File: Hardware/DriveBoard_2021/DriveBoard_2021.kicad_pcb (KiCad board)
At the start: 2 copper layers, 124.5 x 101.6 mm, 91 parts, among them U1 LM2576S-3.3, U2 LM2576HVS-5, U3 TM4C129E_Launchpad, U4 MCP2551-I-SN

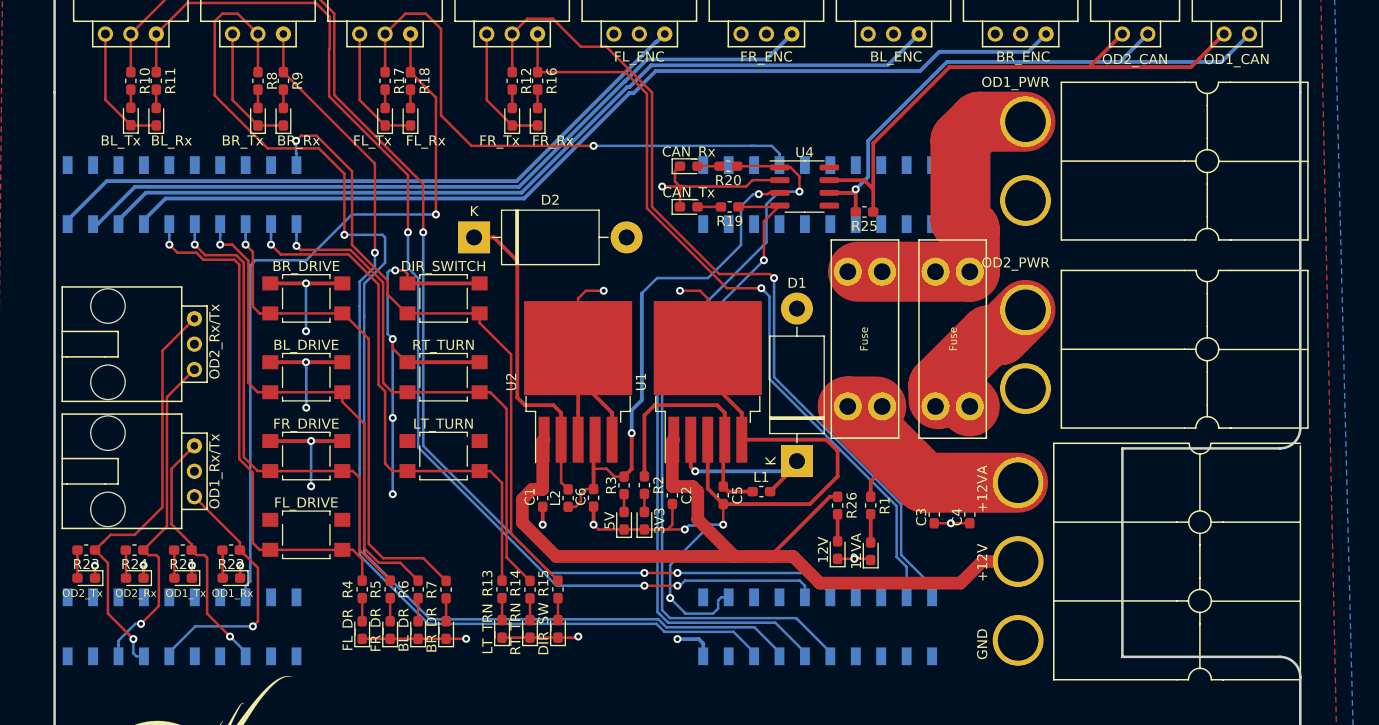
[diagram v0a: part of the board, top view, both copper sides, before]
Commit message: Switched TIVA SMD bottom to THT. Moved Odrive Andersons and re-traced pwr. Added names to LEDs.
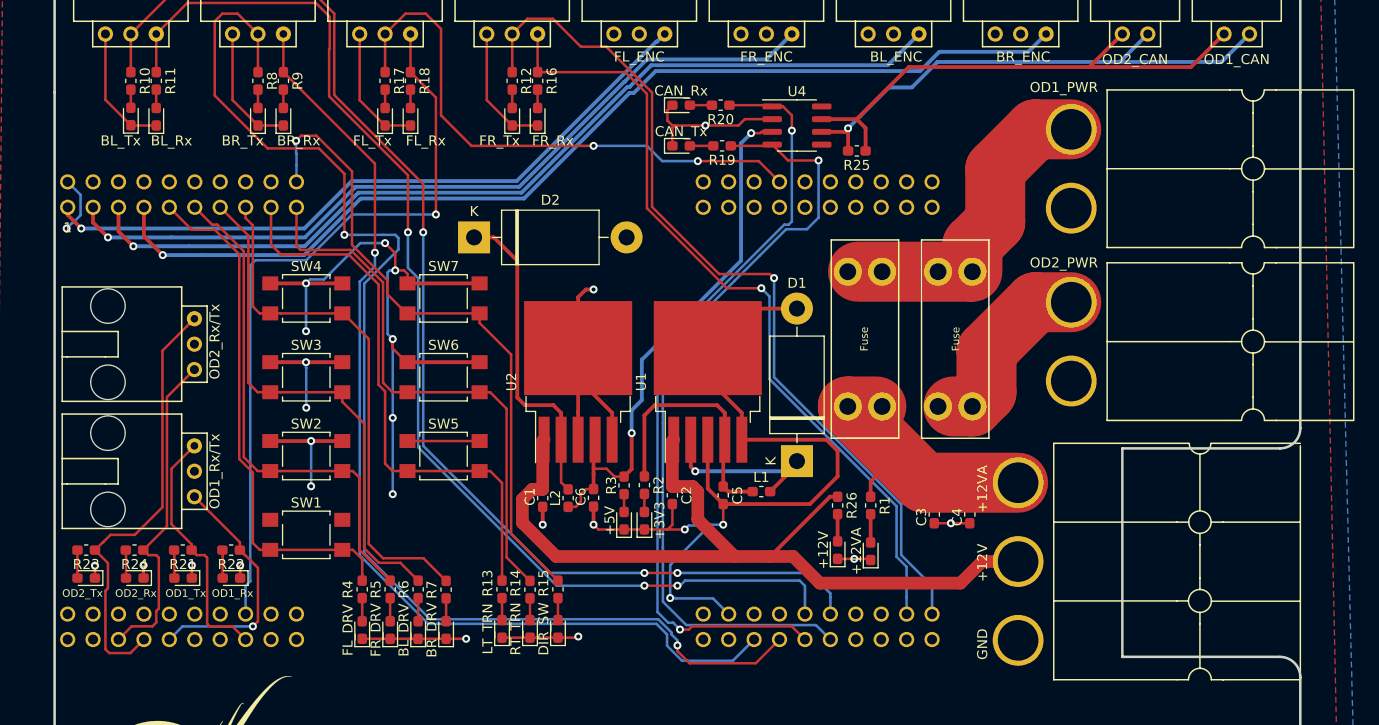
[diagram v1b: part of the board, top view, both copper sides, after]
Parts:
- U3: footprint MRDT_Shields:TM4C129E_Launchpad_FULL_SMD_BOTTOM -> MRDT_Shields:TM4C129E_Launchpad_FULL_THT_BOTTOM
- moved CAN_Tx 6.14 mm to (132.4, 76.7)
- moved R19 6.14 mm to (136.5, 76.7)
- moved R25 6.14 mm to (150.0, 77.2)
- moved U4 6.14 mm to (144.0, 74.7)
- moved CAN_Rx 6.14 mm to (132.4, 72.6)
- moved R20 6.14 mm to (136.4, 72.6)
- moved Conn2 4.64 mm to (175.0, 71.1)
- moved Conn3 4.64 mm to (175.0, 88.4)
- moved F2 0.25 mm to (156.5, 86.1)
- renumbered 12V to +12V, 12VA to +12VA, 3V3 to +3V3, 5V to +5V, BL_DR to BL_DRV, BR_DR to BR_DRV, FL_DR to FL_DRV, FR_DR to FR_DRV, FL_DRIVE to SW1, FR_DRIVE to SW2, BL_DRIVE to SW3, BR_DRIVE to SW4, LT_TURN to SW5, RT_TURN to SW6, DIR_SWITCH to SW7
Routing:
- net +3V3: track 107.8 -> 123.7 mm
- net CAN_Tx: track 68.4 -> 79.6 mm
- net BR_PWM: track 98.2 -> 103.0 mm, vias 0 -> 1
- net GND: track 214.6 -> 219.1 mm
- net CAN_Rx: track 74.0 -> 78.2 mm, vias 1 -> 2
- net CANH: track 55.9 -> 51.9 mm
- net CANL: track 56.9 -> 53.0 mm
- net BL_PWM: track 88.1 -> 91.8 mm, vias 0 -> 1
- net BR_Tx: track 121.6 -> 125.2 mm, vias 1 -> 2
- net FR_PWM: track 77.7 -> 80.4 mm, vias 0 -> 1
- net +5V: track 51.4 -> 53.8 mm
- net OD2_Tx: track 41.7 -> 43.8 mm, vias 1 -> 0
- net RT_TURN: track 54.0 -> 55.6 mm, vias 1 -> 0
- net LT_TURN: track 54.9 -> 56.5 mm, vias 1 -> 0
- net FR_Tx: track 86.5 -> 88.1 mm
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
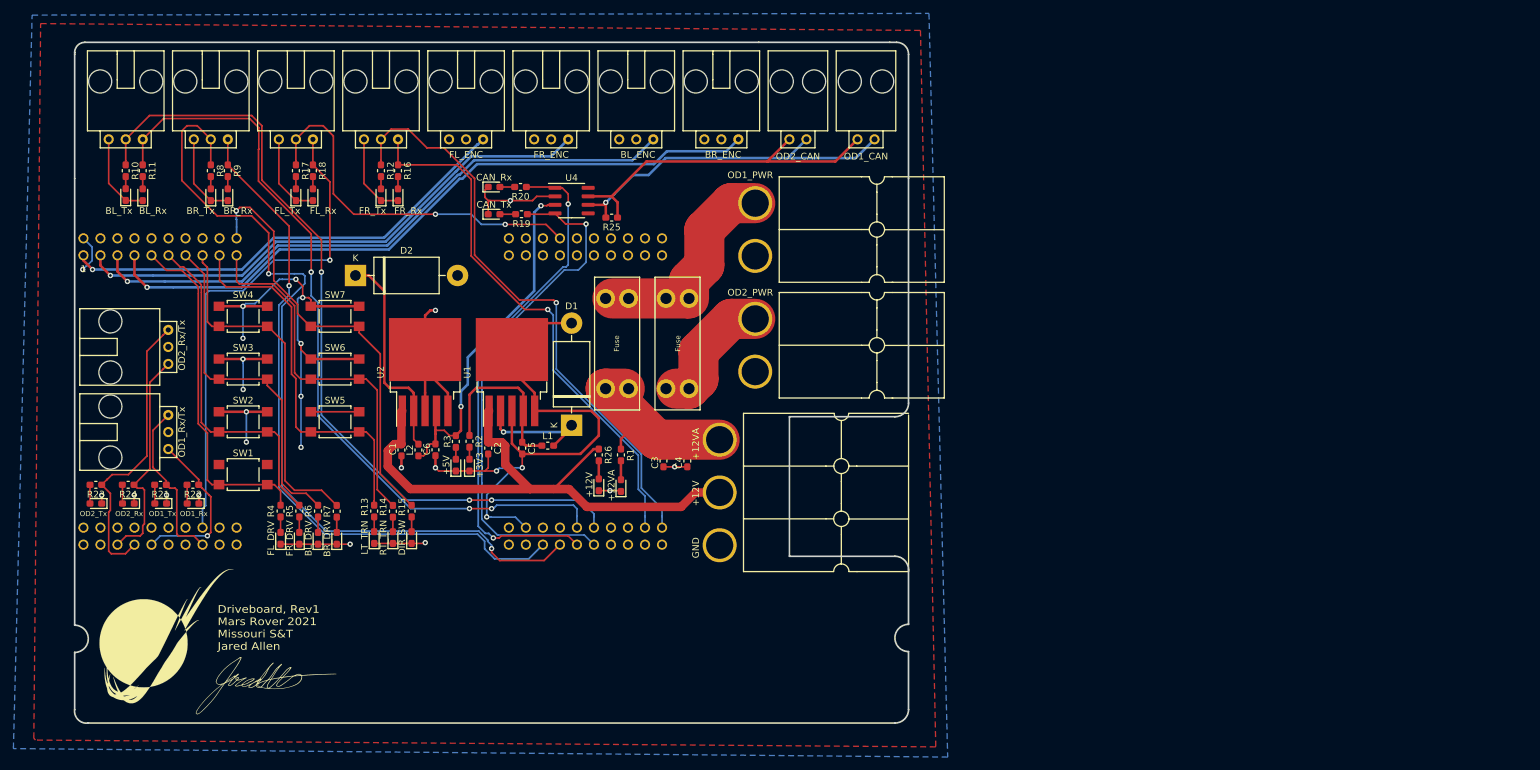
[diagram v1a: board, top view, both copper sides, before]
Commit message: Initial Board Overhaul. Power switched to Okis, re-routing of traces to easier paths. Additional changes.
LEDs given better groupings and silkscreen tags. Given new room with the switch to Okis for regualtors, traces were re-routed to ease the complexity of the board. Odrive trace size changed to 350mil to handle 30A actuation.
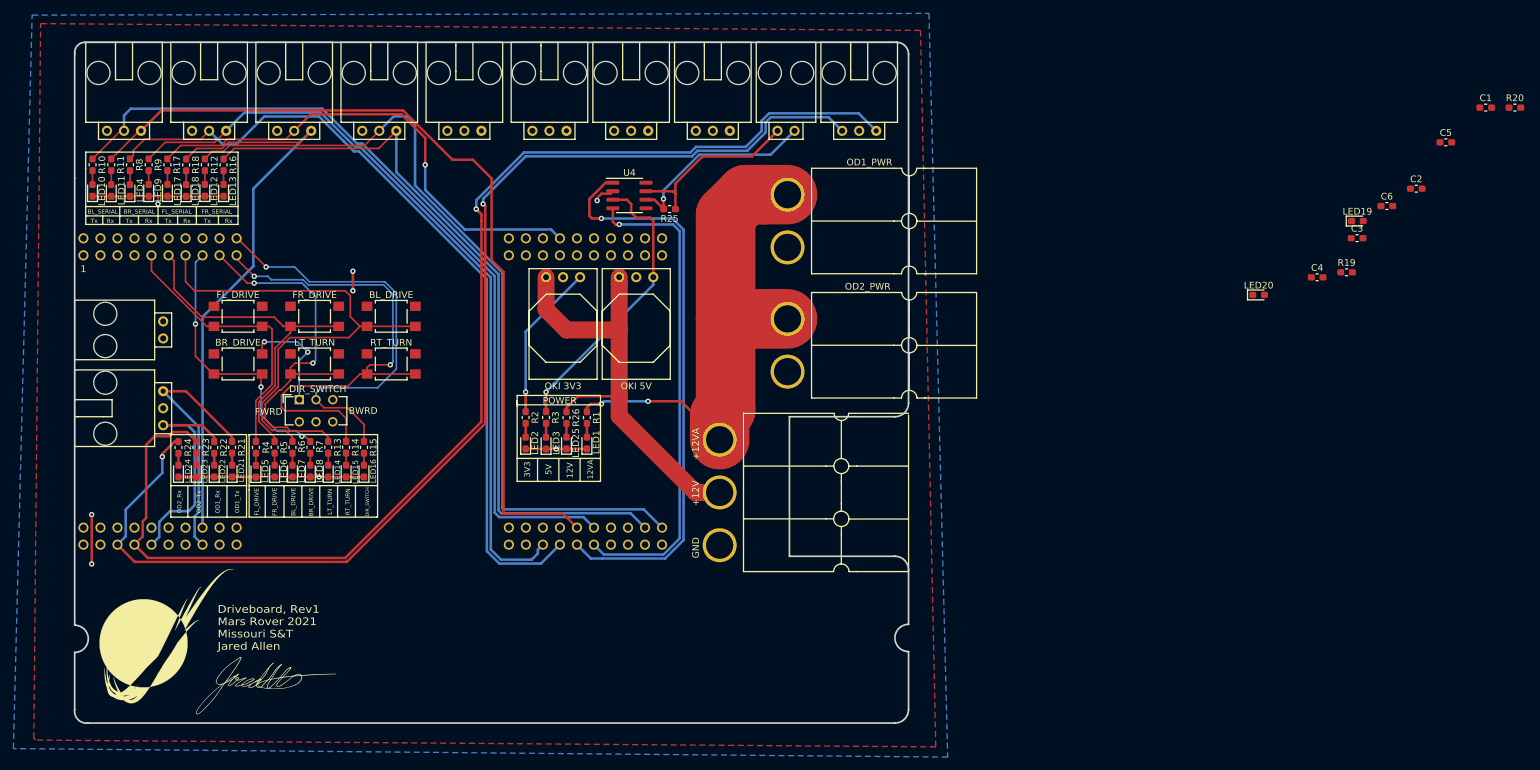
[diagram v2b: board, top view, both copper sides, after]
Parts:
- removed +12V, +12VA, +3V3, +5V: green, LED_SMD:LED_0603_1608Metric_Pad1.05x0.95mm_HandSolder
- removed BL_DRV, BR_DRV, DIR_SW, FL_DRV, FR_DRV, LT_TRN, RT_TRN: yellow, LED_SMD:LED_0603_1608Metric_Pad1.05x0.95mm_HandSolder
- removed BL_Rx, BL_Tx, BR_Rx, BR_Tx, CAN_Rx, CAN_Tx, FL_Rx, FL_Tx, FR_Rx, FR_Tx, OD1_Rx, OD1_Tx, OD2_Rx, OD2_Tx: pink, LED_SMD:LED_0603_1608Metric_Pad1.05x0.95mm_HandSolder
- removed D1, D2: 1N5822, Diode_THT:D_DO-201AD_P15.24mm_Horizontal
- removed F1, F2: Fuse, MRDT_Passives:ATC_Fuse_Block
- removed L1, L2: 100uH, Inductor_SMD:L_0603_1608Metric_Pad1.05x0.95mm_HandSolder
- removed SW1, SW2, SW3, SW4, SW5, SW6, SW7: SW_Push, Button_Switch_SMD:SW_SPST_TL3305A
- added BL_DRIVE: SW_Push, Button_Switch_SMD:SW_SPST_TL3305A, F.Cu at (117.1, 91.9)
- added BR_DRIVE: SW_Push, Button_Switch_SMD:SW_SPST_TL3305A, F.Cu at (94.2, 99.1)
- added DIR_SWITCH: SW_SPST, Button_Switch_THT:SW_CuK_JS202011CQN_DPDT_Straight, F.Cu at (103.4, 104.4)
- added FL_DRIVE: SW_Push, Button_Switch_SMD:SW_SPST_TL3305A, F.Cu at (94.2, 91.9)
- added FR_DRIVE: SW_Push, Button_Switch_SMD:SW_SPST_TL3305A, F.Cu at (105.7, 91.9)
- added LED1: green, LED_SMD:LED_0603_1608Metric_Pad1.05x0.95mm_HandSolder, F.Cu at (146.3, 110.9)
- added LED10: pink, LED_SMD:LED_0603_1608Metric_Pad1.05x0.95mm_HandSolder, F.Cu at (72.5, 73.2)
- added LED11: pink, LED_SMD:LED_0603_1608Metric_Pad1.05x0.95mm_HandSolder, F.Cu at (75.3, 73.2)
- added LED12: pink, LED_SMD:LED_0603_1608Metric_Pad1.05x0.95mm_HandSolder, F.Cu at (89.3, 73.1)
- added LED13: pink, LED_SMD:LED_0603_1608Metric_Pad1.05x0.95mm_HandSolder, F.Cu at (92.1, 73.2)
- added LED14: yellow, LED_SMD:LED_0603_1608Metric_Pad1.05x0.95mm_HandSolder, F.Cu at (107.7, 115.0)
- added LED15: yellow, LED_SMD:LED_0603_1608Metric_Pad1.05x0.95mm_HandSolder, F.Cu at (110.4, 115.0)
- added LED16: yellow, LED_SMD:LED_0603_1608Metric_Pad1.05x0.95mm_HandSolder, F.Cu at (113.0, 115.0)
- added LED17: pink, LED_SMD:LED_0603_1608Metric_Pad1.05x0.95mm_HandSolder, F.Cu at (83.7, 73.1)
- added LED18: pink, LED_SMD:LED_0603_1608Metric_Pad1.05x0.95mm_HandSolder, F.Cu at (86.5, 73.2)
- added LED19: pink, LED_SMD:LED_0603_1608Metric_Pad1.05x0.95mm_HandSolder, F.Cu at (261.3, 77.7)
- added LED2: green, LED_SMD:LED_0603_1608Metric_Pad1.05x0.95mm_HandSolder, F.Cu at (137.2, 110.9)
- added LED20: pink, LED_SMD:LED_0603_1608Metric_Pad1.05x0.95mm_HandSolder, F.Cu at (246.6, 88.8)
- added LED21: pink, LED_SMD:LED_0603_1608Metric_Pad1.05x0.95mm_HandSolder, F.Cu at (93.3, 115.0)
- added LED22: pink, LED_SMD:LED_0603_1608Metric_Pad1.05x0.95mm_HandSolder, F.Cu at (90.7, 115.0)
- added LED23: pink, LED_SMD:LED_0603_1608Metric_Pad1.05x0.95mm_HandSolder, F.Cu at (88.0, 115.0)
- added LED24: pink, LED_SMD:LED_0603_1608Metric_Pad1.05x0.95mm_HandSolder, F.Cu at (85.3, 115.0)
- added LED25: green, LED_SMD:LED_0603_1608Metric_Pad1.05x0.95mm_HandSolder, F.Cu at (143.3, 110.9)
- added LED3: green, LED_SMD:LED_0603_1608Metric_Pad1.05x0.95mm_HandSolder, F.Cu at (140.2, 110.9)
- added LED4: pink, LED_SMD:LED_0603_1608Metric_Pad1.05x0.95mm_HandSolder, F.Cu at (78.1, 73.2)
- added LED5: yellow, LED_SMD:LED_0603_1608Metric_Pad1.05x0.95mm_HandSolder, F.Cu at (96.9, 115.1)
- added LED6: yellow, LED_SMD:LED_0603_1608Metric_Pad1.05x0.95mm_HandSolder, F.Cu at (99.7, 115.0)
- added LED7: yellow, LED_SMD:LED_0603_1608Metric_Pad1.05x0.95mm_HandSolder, F.Cu at (102.4, 115.0)
- added LED8: yellow, LED_SMD:LED_0603_1608Metric_Pad1.05x0.95mm_HandSolder, F.Cu at (105.0, 115.0)
- added LED9: pink, LED_SMD:LED_0603_1608Metric_Pad1.05x0.95mm_HandSolder, F.Cu at (80.9, 73.2)
- added LT_TURN: SW_Push, Button_Switch_SMD:SW_SPST_TL3305A, F.Cu at (105.7, 99.1)
- added RT_TURN: SW_Push, Button_Switch_SMD:SW_SPST_TL3305A, F.Cu at (117.1, 99.1)
- C1, C2: value 100uF -> 10uF
- C5, C6: value 1000uF -> 10uF
- U1: value LM2576S-3.3 -> OKI 3V3; footprint Package_TO_SOT_SMD:TO-263-5_TabPin3 -> MRDT_Devices:OKI_Horizontal
- U2: value LM2576HVS-5 -> OKI 5V; footprint Package_TO_SOT_SMD:TO-263-5_TabPin3 -> MRDT_Devices:OKI_Horizontal
- moved C1 169.7 mm to (280.5, 60.8), turned to 0 degrees
- moved R20 148.9 mm to (284.8, 60.8), turned to 0 degrees
- moved C6 146.6 mm to (265.7, 75.5), turned to 0 degrees
- moved C5 145.2 mm to (274.5, 66.0), turned to 0 degrees
- moved C2 143.8 mm to (270.1, 72.9), turned to 0 degrees
- moved R19 123.5 mm to (259.7, 85.4), turned to 0 degrees
- moved C3 108.7 mm to (261.3, 80.3), turned to 0 degrees
- moved CAN1 108.7 mm to (83.1, 94.0), turned to 90 degrees
- moved SERIAL2 108.1 mm to (186.9, 64.3), turned to 0 degrees
- moved C4 97.9 mm to (255.3, 86.1), turned to 0 degrees
- moved U2 30.6 mm to (148.6, 84.8), turned to 0 degrees
- moved R12 26.3 mm to (89.3, 69.3)
- moved R16 26.0 mm to (92.1, 69.3)
- moved R17 19.2 mm to (83.7, 69.3)
- moved R18 18.9 mm to (86.5, 69.3)
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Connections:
- C2 pad 1: +12V -> +3V3
- C5 pad 1: +3V3 -> +12V
- Conn2 pad 2: Net-(Conn2-Pad2) -> +12VA
- Conn3 pad 2: Net-(Conn3-Pad2) -> +12VA
- U1 pad 2: Net-(D1-Pad1) -> GND
- U1 pad 3: GND -> +3V3
- U2 pad 2: Net-(D2-Pad1) -> GND
- U2 pad 3: GND -> +5V
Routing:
- net GND: track 219.1 -> 63.7 mm, vias 16 -> 6
- net OD2_Rx: track 33.1 -> 178.0 mm, vias 0 -> 2
- net OD2_Tx: track 43.8 -> 185.9 mm, vias 0 -> 1
- net BR_PWM: track 103.0 -> 0.00 mm, vias 1 -> 0
- net BL_PWM: track 91.8 -> 0.00 mm, vias 1 -> 0
- net FR_PWM: track 80.4 -> 0.00 mm, vias 1 -> 0
- net +3V3: track 123.7 -> 47.5 mm, vias 11 -> 5
- net FL_PWM: track 69.0 -> 0.00 mm, vias 1 -> 0
- net +12VA: track 29.0 -> 75.4 mm, vias 0 -> 2
- net FR_Tx: track 88.1 -> 122.3 mm, vias 1 -> 0
- net FR_Rx: track 80.4 -> 113.4 mm, vias 1 -> 0
- net Net-(D2-Pad1): track 31.9 -> 0.00 mm
- net Net-(Conn2-Pad2): track 31.6 -> 0.00 mm
- net CANH: track 51.9 -> 26.9 mm
- net CANL: track 53.0 -> 29.3 mm
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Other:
- board text added: "12V"
- board text added: "12VA"
- board text added: "3V3"
- board text added: "5V"
- board text added: "BL_DRIVE"
- board text added: "BL_SERIAL"
- board text added: "BR_DRIVE"
- board text added: "BR_SERIAL"
- board text added: "BWRD"
- board text added: "DIR_SWITCH"
- board text added: "FL_DRIVE"
- board text added: "FL_SERIAL"
- board text added: "FR_DRIVE"
- board text added: "FR_SERIAL"
- board text added: "FWRD"
- board text added: "LT_TURN"
- board text added: "OD1_Rx"
- board text added: "OD1_Tx"
- board text added: "OD2_Rx"
- board text added: "OD2_Tx"
- board text added: "POWER"
- board text added: "RT_TURN"
- board text added: "Rx"
- board text added: "Tx"
- board text removed: "BL_ENC"
- board text removed: "BR_ENC"
- board text removed: "FL_ENC"
- board text removed: "FR_ENC"
- board text removed: "OD1_CAN"
- board text removed: "OD1_Rx/Tx"
- board text removed: "OD2_CAN"
- board text removed: "OD2_Rx/Tx"

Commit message: All Components and Traces Placed
Finished updating schematic to meet CDR changes.
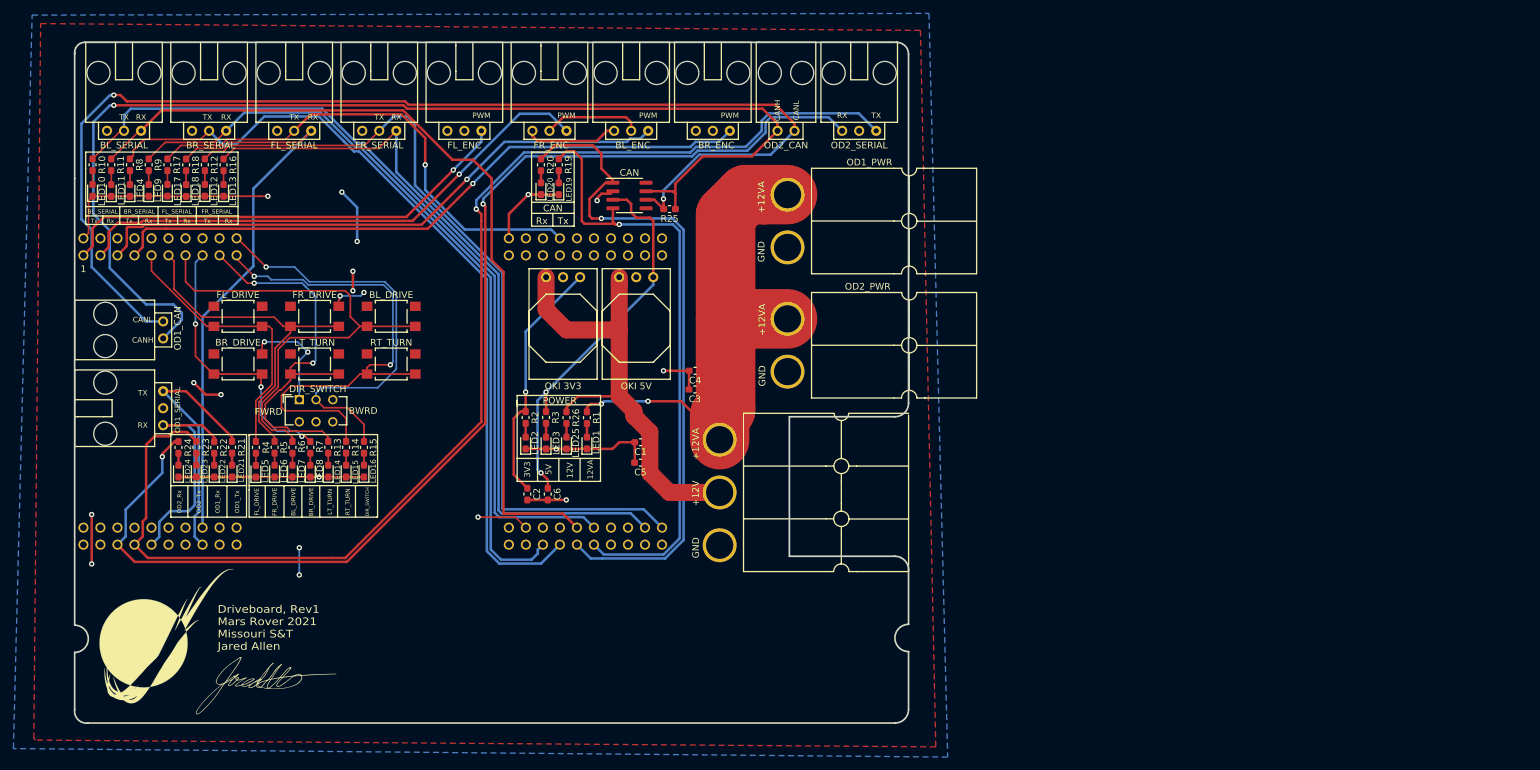
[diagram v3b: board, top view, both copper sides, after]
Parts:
- moved R20 145.6 mm to (139.4, 69.3), turned to 270 degrees
- moved C2 140.3 mm to (137.4, 118.5), turned to 270 degrees
- moved C1 135.7 mm to (154.3, 110.7), turned to 180 degrees
- moved C6 132.4 mm to (140.5, 118.5), turned to 270 degrees
- moved C5 129.4 mm to (154.3, 113.8), turned to 180 degrees
- moved LED19 119.3 mm to (142.1, 72.9), turned to 90 degrees
- moved R19 118.7 mm to (142.1, 69.3), turned to 270 degrees
- moved LED20 108.3 mm to (139.4, 72.9), turned to 90 degrees
- moved C3 101.4 mm to (162.4, 102.9), turned to 180 degrees
- moved C4 93.9 mm to (162.4, 100.1), turned to 180 degrees
- renumbered U4 to CAN
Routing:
- net CANL: track 29.3 -> 176.3 mm, vias 1 -> 2
- net CANH: track 26.9 -> 173.5 mm, vias 0 -> 1
- net BR_PWM: track 0.00 -> 97.9 mm, vias 0 -> 1
- net BL_PWM: track 0.00 -> 88.5 mm, vias 0 -> 1
- net FR_PWM: track 0.00 -> 80.7 mm, vias 0 -> 1
- net GND: track 63.7 -> 138.7 mm, vias 6 -> 12
- net FL_PWM: track 0.00 -> 69.6 mm, vias 0 -> 1
- net +3V3: track 47.5 -> 92.6 mm, vias 5 -> 11
- net CAN_Tx: track 72.8 -> 91.7 mm
- net +5V: track 43.2 -> 58.7 mm, vias 1 -> 2
- net CAN_Rx: track 86.2 -> 101.6 mm
- net +12V: track 66.7 -> 68.9 mm
- net Net-(LED19-Pad2): track 0.00 -> 1.83 mm
- net Net-(LED20-Pad2): track 0.00 -> 1.81 mm
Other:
- board text added: "BL_ENC"
- board text added: "BR_ENC"
- board text added: "CAN"
- board text added: "CANH"
- board text added: "CANL"
- board text added: "FL_ENC"
- board text added: "FR_ENC"
- board text added: "OD1_CAN"
- board text added: "OD1_SERIAL"
- board text added: "OD2_CAN"
- board text added: "OD2_SERIAL"
- board text added: "PWM"
- board text added: "RX"
- board text added: "TX"
